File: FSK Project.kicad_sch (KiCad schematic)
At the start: 47 parts, among them J1 DATA IN, J2 TX_PAIR, J3 RX_PAIR, J4 DATA_OUT, Q1 2N3904, Q2 2N3904, SW1 MAN, U1 MC14046BCP, U2 LM393, U3 MC14046BCP

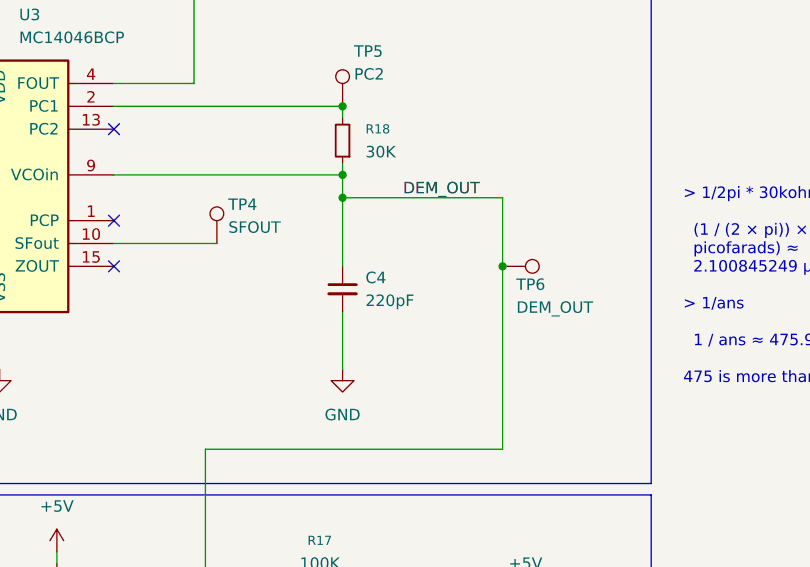
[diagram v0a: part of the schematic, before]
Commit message: Add page 5 filter information
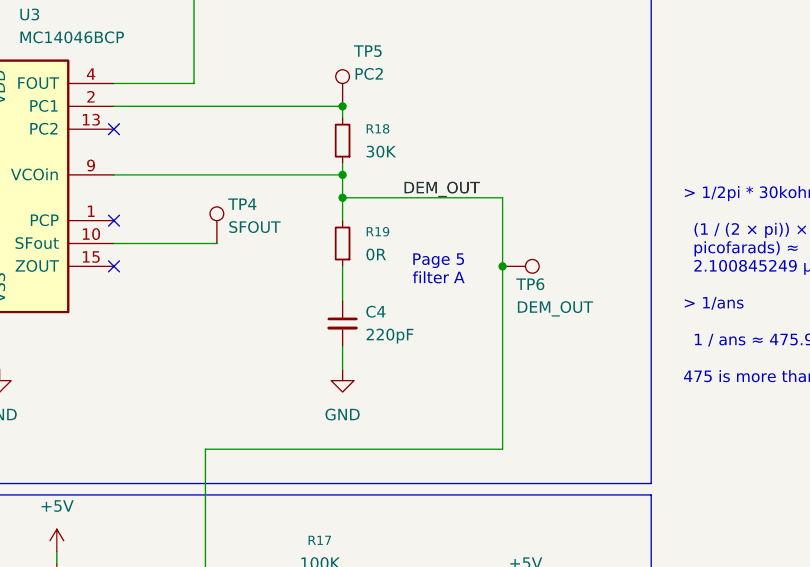
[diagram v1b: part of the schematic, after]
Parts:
- added R19: 0R, Resistor_THT:R_Axial_DIN0204_L3.6mm_D1.6mm_P7.62mm_Horizontal, symbol Device:R_Small
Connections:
- net DEM_OUT: now also R19.2; no longer C4.1
- new net: C4.1, R19.1
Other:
- note added: "Page 5 filter A"
- moved on the sheet: C4
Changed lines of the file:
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@@
 		)
 	)
+	(text "Page 5\nfilter A"
+		(exclude_from_sim no)
+		(at 260.858 74.168 0)
+		(effects
+			(font
+				(size 1.27 1.27)
+			)
+		)
+	)
 	(text "Sets Max"
 		(exclude_from_sim no)
@@
 	)
 	(junction
+		(at 250.19 66.04)
+		(diameter 0)
+		(color 0 0 0 0)
+	)
+	(junction
 		(at 45.72 130.81)
 		(diameter 0)
@@
 		(color 0 0 0 0)
 	)
-	(junction
-		(at 250.19 66.04)
-		(diameter 0)
-		(color 0 0 0 0)
-	)
 	(no_connect
 		(at 24.13 133.35)
@@
 	(wire
 		(pts
-			(xy 250.19 66.04) (xy 250.19 73.66)
+			(xy 250.19 66.04) (xy 250.19 68.58)
 		)
 		(stroke
@@
 	(wire
 		(pts
-			(xy 250.19 78.74) (xy 250.19 85.09)
+			(xy 250.19 82.55) (xy 250.19 85.09)
 		)
 		(stroke
@@
 	(wire
 		(pts
+			(xy 250.19 73.66) (xy 250.19 77.47)
+		)
+		(stroke
+			(width 0)
+			(type default)
+		)
+	)
+	(wire
+		(pts
 			(xy 120.65 86.36) (xy 120.65 55.88)
 		)
@@
 	)
 	(symbol
+		(lib_id "Device:R_Small")
+		(at 250.19 71.12 180)
+		(unit 1)
+		(body_style 1)
+		(exclude_from_sim no)
+		(in_bom yes)
+		(on_board yes)
+		(in_pos_files yes)
+		(dnp no)
+		(fields_autoplaced yes)
+		(property "Reference" "R19"
+			(at 252.73 69.8499 0)
+			(show_name no)
+			(do_not_autoplace no)
+			(effects
+				(font
+					(size 1.016 1.016)
+				)
+				(justify right)
+			)
+		)
+		(property "Value" "0R"
+			(at 252.73 72.3899 0)
+			(show_name no)
+			(do_not_autoplace no)
+			(effects
+				(font
+					(size 1.27 1.27)
+				)
+				(justify right)
+			)
+		)
+		(property "Footprint" "Resistor_THT:R_Axial_DIN0204_L3.6mm_D1.6mm_P7.62mm_Horizontal"
+			(at 250.19 71.12 0)
+			(hide yes)
+			(show_name no)
+			(do_not_autoplace no)
+			(effects
+				(font
+					(size 1.27 1.27)
+				)
+			)
+		)
+		(property "Datasheet" ""
+			(at 250.19 71.12 0)
+			(hide yes)
+			(show_name no)
+			(do_not_autoplace no)
+			(effects
+				(font
+					(size 1.27 1.27)
+				)
+			)
+		)
+		(property "Description" "Resistor, small symbol"
+			(at 250.19 71.12 0)
+			(hide yes)
+			(show_name no)
+			(do_not_autoplace no)
+			(effects
+				(font
+					(size 1.27 1.27)
+				)
+			)
+		)
+		(pin "1"
+		)
+		(pin "2"
+		)
+		(instances
+			(project "FSK Project"
+				(path "/504c4446-9b80-4e4d-8632-780930dde7a1"
+					(reference "R19")
+					(unit 1)
+				)
+			)
+		)
+	)
+	(symbol
 		(lib_id "Connector:TestPoint")
 		(at 46.99 130.81 0)
@@
 	(symbol
 		(lib_id "Device:C_Small")
-		(at 250.19 76.2 0)
+		(at 250.19 80.01 0)
 		(unit 1)
 		(body_style 1)
@@
 		(fields_autoplaced yes)
 		(property "Reference" "C4"
-			(at 252.73 74.9362 0)
+			(at 252.73 78.7462 0)
 			(show_name no)
 			(do_not_autoplace no)
@@
 		)
 		(property "Value" "220pF"
-			(at 252.73 77.4762 0)
+			(at 252.73 81.2862 0)
 			(show_name no)
 			(do_not_autoplace no)
@@
 		)
 		(property "Footprint" "Capacitor_THT:C_Disc_D6.0mm_W2.5mm_P5.00mm"
-			(at 250.19 76.2 0)
+			(at 250.19 80.01 0)
 			(hide yes)
 			(show_name no)
@@
 		)
 		(property "Datasheet" ""
-			(at 250.19 76.2 0)
+			(at 250.19 80.01 0)
 			(hide yes)
 			(show_name no)
@@
 		)
 		(property "Description" "Unpolarized capacitor, small symbol"
-			(at 250.19 76.2 0)
+			(at 250.19 80.01 0)
 			(hide yes)
 			(show_name no)

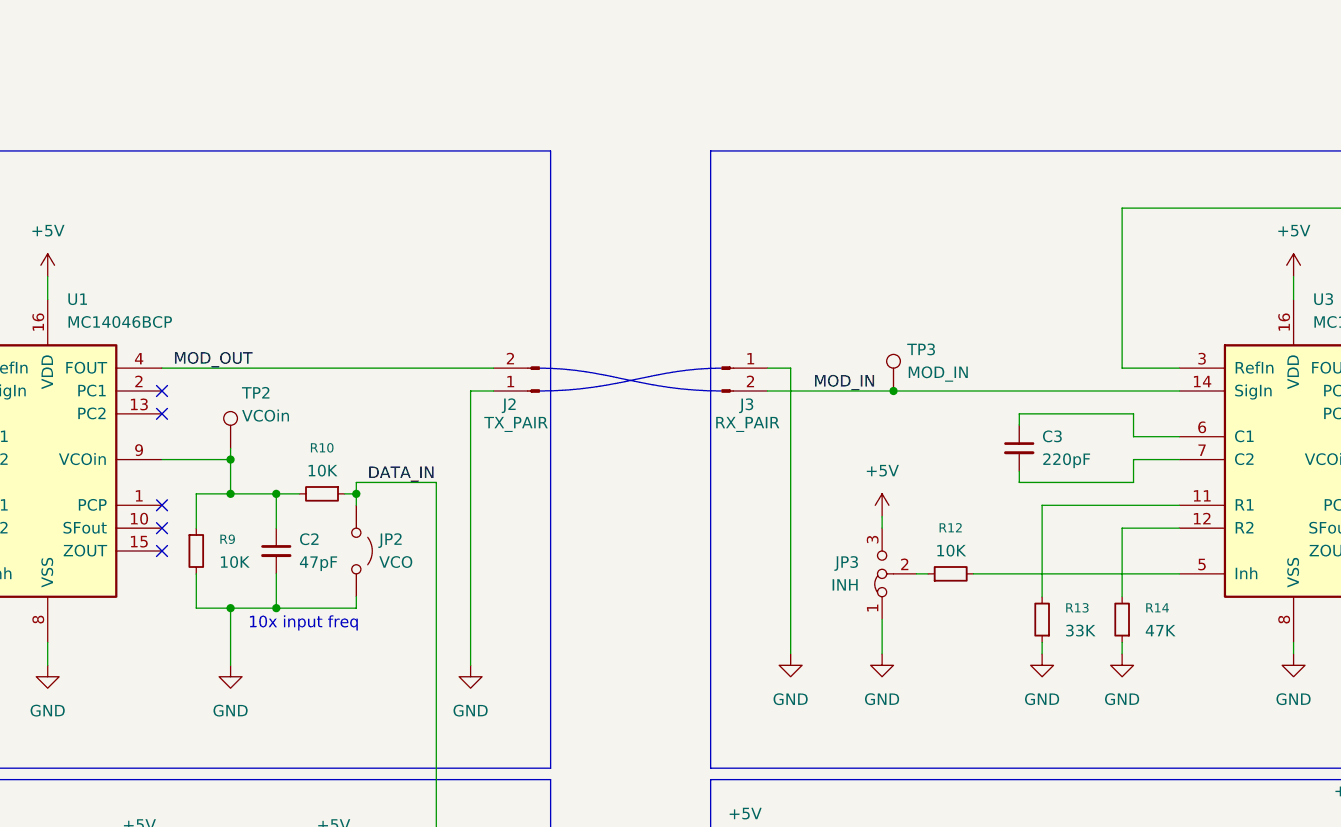
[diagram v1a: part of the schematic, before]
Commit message: Add static protection
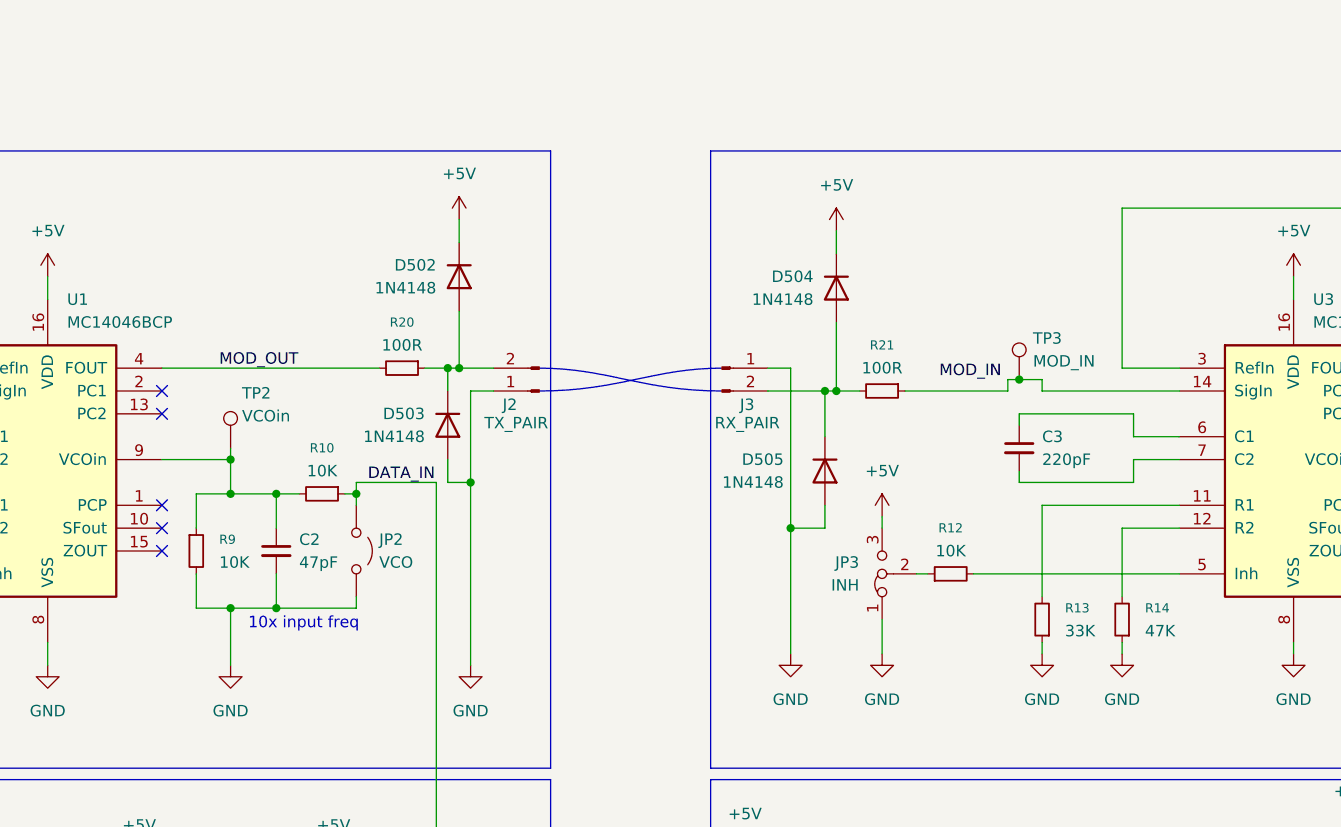
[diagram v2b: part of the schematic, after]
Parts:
- added D502, D503, D504, D505: 1N4148, Diode_THT:D_DO-35_SOD27_P7.62mm_Horizontal, symbol Diode:1N4148
- added R20, R21: 100R, Resistor_THT:R_Axial_DIN0204_L3.6mm_D1.6mm_P7.62mm_Horizontal, symbol Device:R_Small
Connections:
- net +5V: now also D502.1 (K), D504.1 (K)
- net GND: now also D503.2 (A), D505.2 (A)
- net MOD_IN: no longer J3.2 (Pin_2), TP3.1, U3.14 (SigIn)
- net MOD_OUT: now also R20.2; no longer J2.2 (Pin_2)
- new net: R21.1, TP3.1, U3.14 (SigIn)
- new net: D504.2 (A), D505.1 (K), J3.2 (Pin_2), R21.2
- new net: D502.2 (A), D503.1 (K), J2.2 (Pin_2), R20.1
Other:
- moved on the sheet: TP3

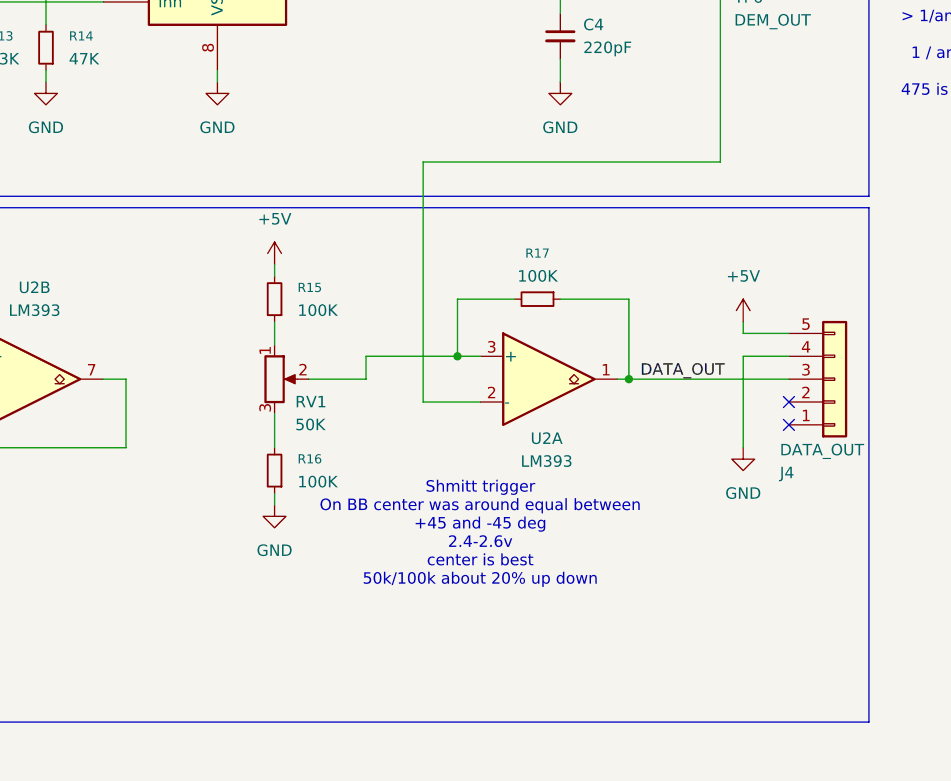
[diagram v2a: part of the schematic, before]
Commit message: Add final libs, include last leftover bits, fix op-amp and verify on board
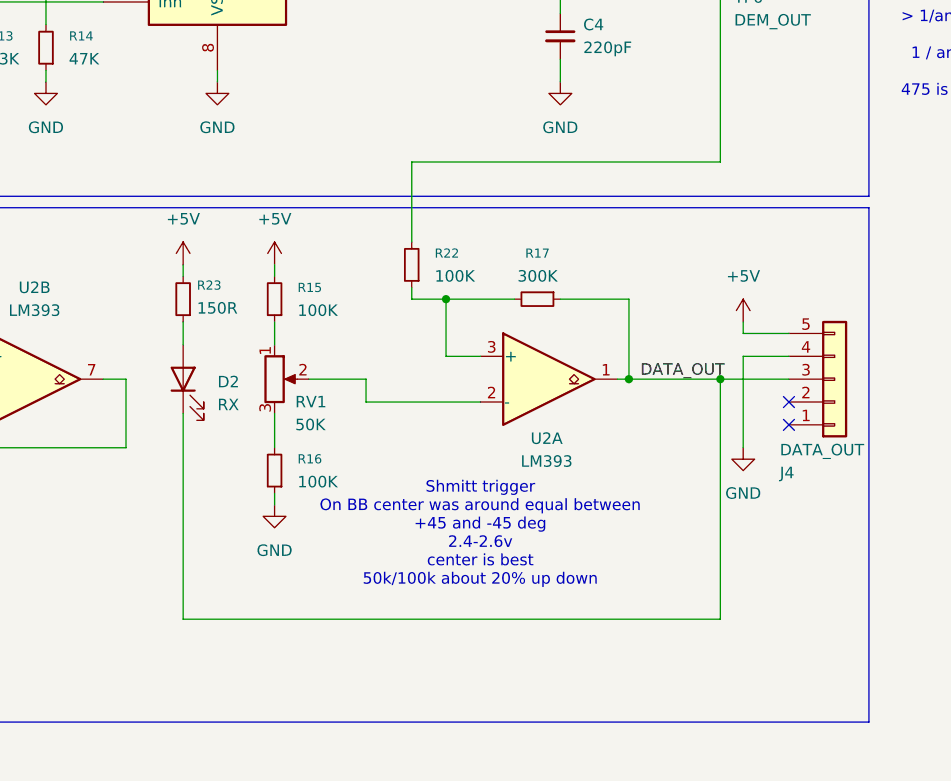
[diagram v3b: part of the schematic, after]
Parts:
- added D2: RX, LED_THT:LED_D3.0mm, symbol Device:LED
- added R22: 100K, Resistor_THT:R_Axial_DIN0204_L3.6mm_D1.6mm_P7.62mm_Horizontal, symbol Device:R_Small
- added R23: 150R, Resistor_THT:R_Axial_DIN0204_L3.6mm_D1.6mm_P7.62mm_Horizontal, symbol Device:R_Small
- R17: value 100K -> 300K
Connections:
- net +5V: now also R23.2
- net DATA_OUT: now also D2.1 (K)
- net DEM_OUT: now also R22.2; no longer U2.2 (-)
- net at R17.2, U2.3 (+): now also R22.1; no longer RV1.2
- new net: RV1.2, U2.2 (-)
- new net: D2.2 (A), R23.1

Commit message: Export gerbers
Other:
- note added: "10K and 30K inital 100K and 300K less loading max output from PPL is very small"
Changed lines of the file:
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@@
+		)
+	)
+	(text "10K and 30K inital\n100K and 300K less loading\nmax output from PPL is very small"
+		(exclude_from_sim no)
+		(at 249.428 99.822 0)
+		(effects
+			(font
+				(size 1.27 1.27)
+			)
+			(justify left top)
 		)
 	)

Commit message: fix some issues i made in the design oops
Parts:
- R13, R3: value 33K -> 100k
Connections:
- net MOD_IN: now also R21.1, TP3.1, U3.3 (RefIn)
- net at U3.4 (FOUT): now also U3.14 (SigIn); no longer U3.3 (RefIn)
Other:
- moved on the sheet: TP3
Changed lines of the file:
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@@
 	)
 	(junction
-		(at 181.61 54.61)
+		(at 237.49 109.22)
 		(diameter 0)
 		(color 0 0 0 0)
 	)
 	(junction
-		(at 237.49 109.22)
+		(at 99.06 67.31)
 		(diameter 0)
 		(color 0 0 0 0)
 	)
 	(junction
-		(at 99.06 67.31)
+		(at 182.88 53.34)
 		(diameter 0)
 		(color 0 0 0 0)
@@
 	(wire
 		(pts
-			(xy 184.15 54.61) (xy 184.15 55.88)
-		)
-		(stroke
-			(width 0)
-			(type default)
-		)
-	)
-	(wire
-		(pts
 			(xy 90.17 76.2) (xy 90.17 80.01)
 		)
@@
 	(wire
 		(pts
-			(xy 199.39 53.34) (xy 193.04 53.34)
-		)
-		(stroke
-			(width 0)
-			(type default)
-		)
-	)
-	(wire
-		(pts
 			(xy 118.11 66.04) (xy 120.65 66.04)
 		)
@@
 	(wire
 		(pts
-			(xy 193.04 53.34) (xy 193.04 35.56)
-		)
-		(stroke
-			(width 0)
-			(type default)
-		)
-	)
-	(wire
-		(pts
 			(xy 218.44 111.76) (xy 218.44 114.3)
 		)
@@
 	(wire
 		(pts
+			(xy 193.04 55.88) (xy 199.39 55.88)
+		)
+		(stroke
+			(width 0)
+			(type default)
+		)
+	)
+	(wire
+		(pts
 			(xy 176.53 76.2) (xy 199.39 76.2)
 		)
@@
 	(wire
 		(pts
-			(xy 180.34 54.61) (xy 181.61 54.61)
+			(xy 180.34 53.34) (xy 182.88 53.34)
 		)
 		(stroke
@@
 	(wire
 		(pts
-			(xy 180.34 54.61) (xy 180.34 55.88)
+			(xy 180.34 53.34) (xy 180.34 55.88)
 		)
 		(stroke
@@
 	(wire
 		(pts
-			(xy 181.61 54.61) (xy 184.15 54.61)
-		)
-		(stroke
-			(width 0)
-			(type default)
-		)
-	)
-	(wire
-		(pts
 			(xy 83.82 129.54) (xy 83.82 149.86)
 		)
@@
 	(wire
 		(pts
+			(xy 193.04 35.56) (xy 193.04 55.88)
+		)
+		(stroke
+			(width 0)
+			(type default)
+		)
+	)
+	(wire
+		(pts
 			(xy 267.97 66.04) (xy 267.97 73.66)
 		)
@@
 	(wire
 		(pts
+			(xy 182.88 53.34) (xy 199.39 53.34)
+		)
+		(stroke
+			(width 0)
+			(type default)
+		)
+	)
+	(wire
+		(pts
 			(xy 160.02 68.58) (xy 160.02 71.12)
 		)
@@
 	(wire
 		(pts
-			(xy 184.15 55.88) (xy 199.39 55.88)
-		)
-		(stroke
-			(width 0)
-			(type default)
-		)
-	)
-	(wire
-		(pts
 			(xy 257.81 109.22) (xy 257.81 118.11)
 		)
@@
 	)
 	(label "MOD_IN"
-		(at 172.72 54.61 0)
+		(at 171.45 55.88 0)
 		(effects
 			(font
@@
 			)
 		)
-		(property "Value" "33K"
+		(property "Value" "100k"
 			(at 186.69 82.5499 0)
 			(show_name no)
@@
 			)
 		)
-		(property "Value" "33K"
+		(property "Value" "100k"
 			(at 46.736 82.296 0)
 			(show_name no)
@@
 	(symbol
 		(lib_id "Connector:TestPoint")
-		(at 181.61 54.61 0)
+		(at 182.88 53.34 0)
 		(unit 1)
 		(body_style 1)
@@
 		(dnp no)
 		(property "Reference" "TP3"
-			(at 183.134 50.038 0)
+			(at 184.404 48.768 0)
 			(show_name no)
 			(do_not_autoplace no)
@@
 		)
 		(property "Value" "MOD_IN"
-			(at 183.134 52.578 0)
+			(at 184.404 51.308 0)
 			(show_name no)
 			(do_not_autoplace no)
@@
 		)
 		(property "Footprint" "TestPoint:TestPoint_Loop_D2.54mm_Drill1.5mm_Beaded"
-			(at 186.69 54.61 0)
+			(at 187.96 53.34 0)
 			(hide yes)
 			(show_name no)
@@
 		)
 		(property "Datasheet" ""
-			(at 186.69 54.61 0)
+			(at 187.96 53.34 0)
 			(hide yes)
 			(show_name no)
@@
 		)
 		(property "Description" "test point"
-			(at 181.61 54.61 0)
+			(at 182.88 53.34 0)
 			(hide yes)
 			(show_name no)

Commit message: Finish before class
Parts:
- R18: value 30K -> 33K
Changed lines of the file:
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@@
 			)
 		)
-		(property "Value" "30K"
+		(property "Value" "33K"
 			(at 252.73 60.9599 0)
 			(show_name no)
